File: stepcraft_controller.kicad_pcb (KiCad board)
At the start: 2 copper layers, 68 x 55 mm, 70 parts, among them J1 USB, J10 4th Axle, J11 Input2 Select, J2 Probe, J3 Spindle, J4 OutSelect, J6 Relay select, J7 Serial, J8 ISP, J9 X1, SW1 RST, U1 CP2102N-A01-GQFN24, U2 ADuM1201BR, U3 ADuM1201BR, U4 ATMEGA328P-AU, Y1 Crystal

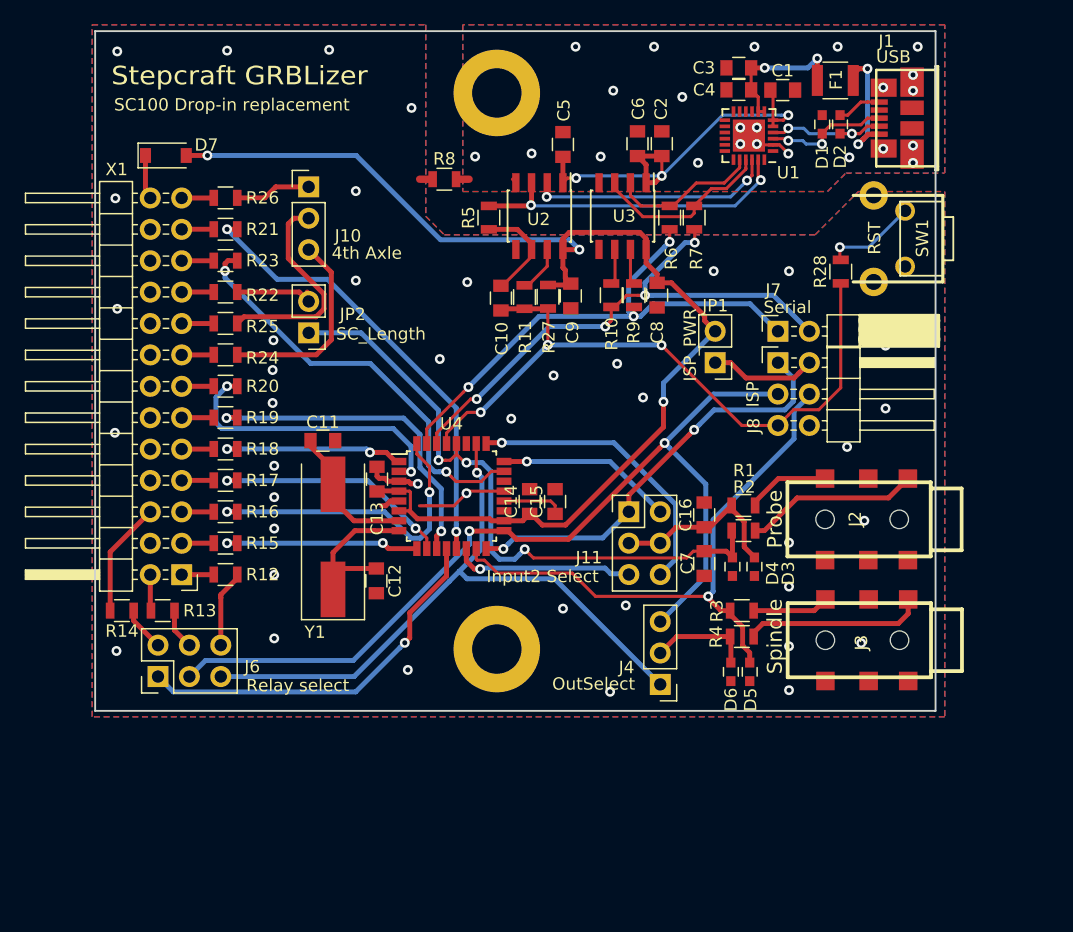
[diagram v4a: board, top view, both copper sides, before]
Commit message: Fix Diode symbol (was reversed), input dcouple caps value, X1 caps value, minor routing improvement.
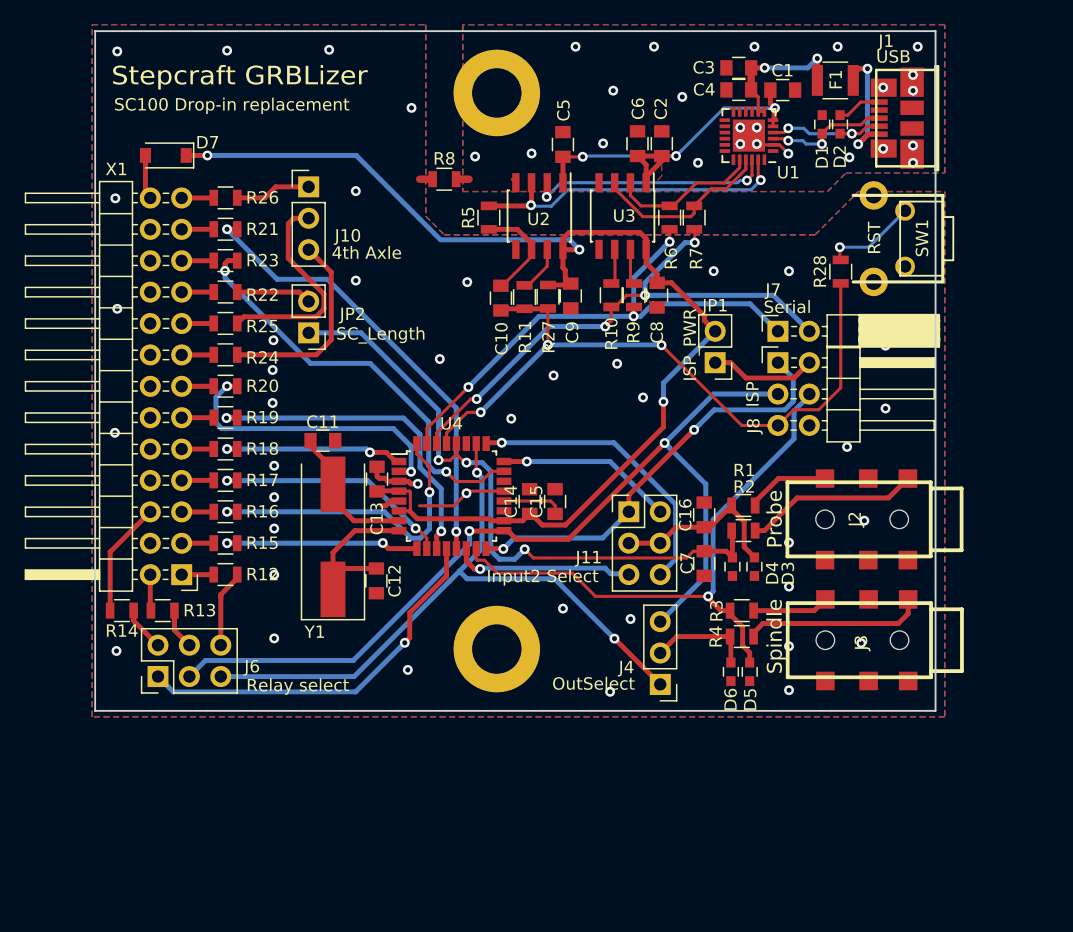
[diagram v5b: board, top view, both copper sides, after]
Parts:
- C11, C12: value 100n -> 22p
- C16, C7: value 100n -> 10n
- D7: value SCHOTTKY -> D_Schottky
- turned D7 to 180 degrees
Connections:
- D7 pad 1: /SC_VCC_5V -> +5V
- D7 pad 2: +5V -> /SC_VCC_5V
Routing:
- net +5VP: track 35.5 -> 32.9 mm
- net /A3: vias 1 -> 2

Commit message: Fix TRS jack pinning Improve some of the scuffy routing...
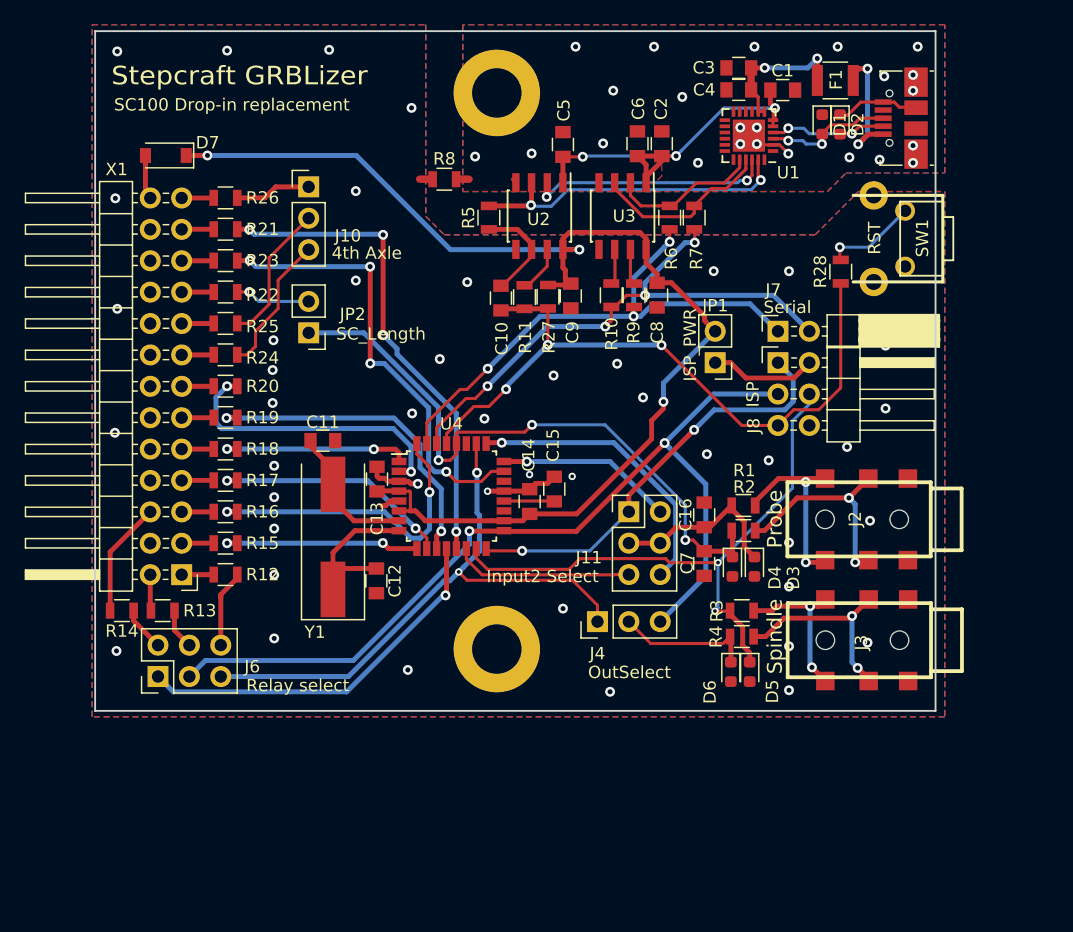
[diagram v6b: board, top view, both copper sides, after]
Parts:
- D1, D2, D3, D4, D5, D6: value D_TVS -> TVS Diode; footprint Capacitors_SMD:C_0603 -> Diode_SMD:D_0603_1608Metric
- J1: footprint iotta_footprints:conn_usb_B_micro_smd -> iotta_footprints:USB_Micro-B_2_Holes
- moved J4 7.18 mm to (180.6, 132.8), turned to 90 degrees
- moved C15 1.01 mm to (177.2, 122.1)
- moved J1 0.88 mm to (205.2, 92.1)
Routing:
- net Net-(J2-Pad2): track 6.73 -> 15.2 mm, vias 0 -> 2
- net Net-(J3-Pad2): track 6.18 -> 12.7 mm, vias 0 -> 2
- net /A3: track 54.2 -> 47.6 mm
- net Net-(J10-Pad2): track 17.4 -> 11.5 mm
- net Net-(J10-Pad3): track 16.2 -> 11.4 mm
- net Net-(J2-Pad1): track 14.1 -> 17.5 mm, vias 0 -> 2
- net /D9: track 36.7 -> 39.8 mm, vias 2 -> 4
- net /SpinDir/Cool: track 8.64 -> 11.6 mm
- net GND: track 7.93 -> 10.8 mm
- net /A0: track 34.1 -> 36.7 mm, vias 2 -> 4
- net /A5: track 53.4 -> 51.5 mm
- net Net-(J3-Pad1): track 14.6 -> 16.4 mm, vias 0 -> 2
- net GNDD: track 14.7 -> 13.3 mm, vias 41 -> 45
- net Net-(C15-Pad1): track 5.03 -> 4.08 mm
- net +5V: track 99.2 -> 98.4 mm
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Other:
- board text added: "Rev 1.1 2017-2022"
- board text removed: "Rev 1.0 2017"

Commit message: Some more minor routing improvements
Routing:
- net +5V: track 98.4 -> 103.4 mm, vias 3 -> 5
- net /D13_SCK: track 75.1 -> 80.0 mm, vias 2 -> 3
- net /A2: track 23.6 -> 21.4 mm
- net /A1: track 14.3 -> 15.5 mm
- net GNDD: vias 45 -> 54
- net /AVR_TX: vias 3 -> 4

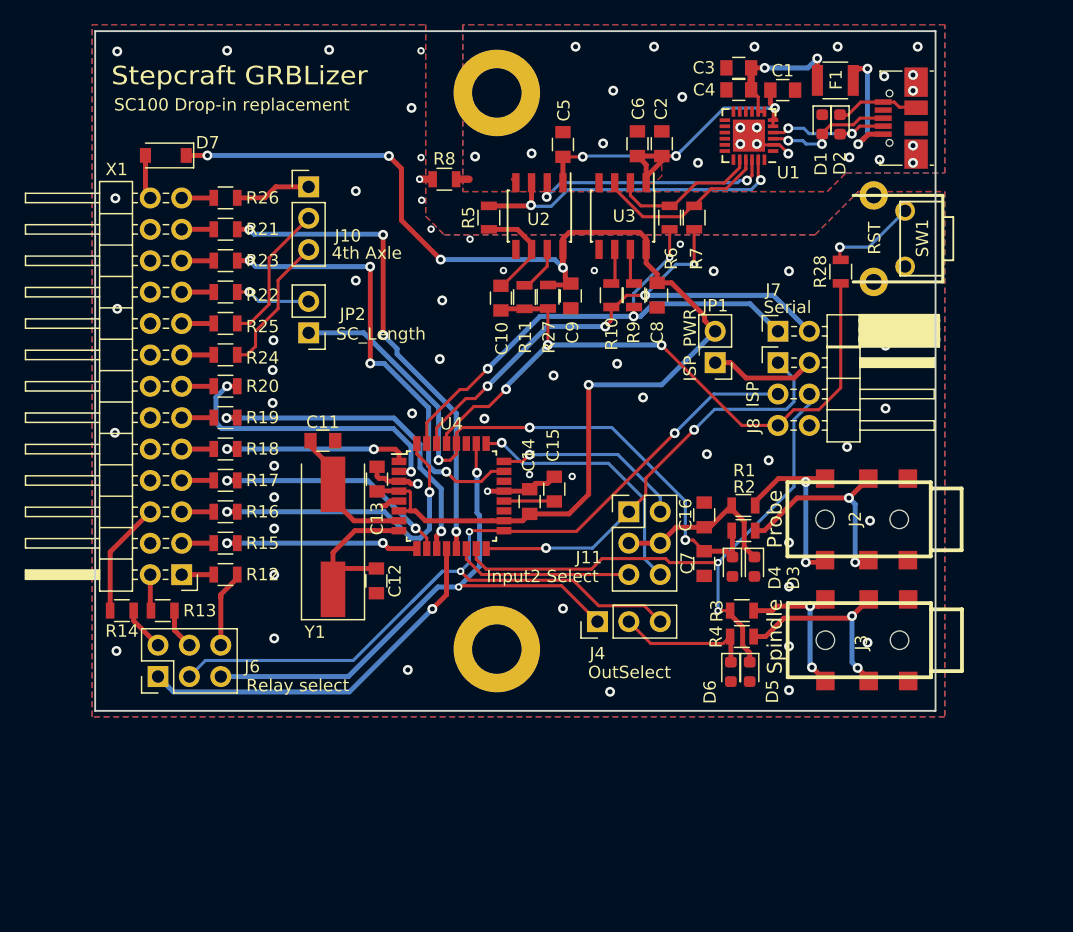
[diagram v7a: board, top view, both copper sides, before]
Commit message: Update project to KiCad v8
- remove all references to external footprints/symbols (close issue #3)
- update footprints to new standard footprint
- add components mgf partnos and LCSC part# for all non standard parts
- shrink PCB outline by 2x0.25mm (for a better fit in machine)
- improve routing
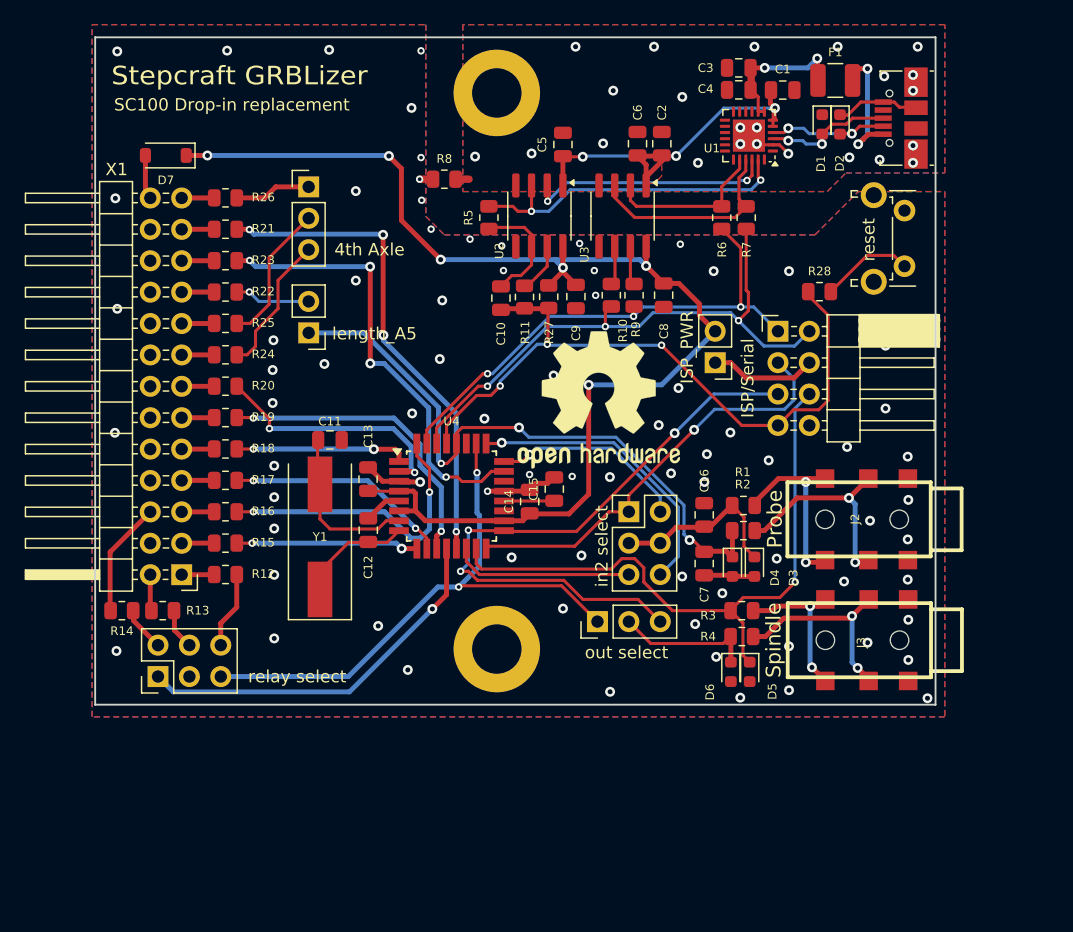
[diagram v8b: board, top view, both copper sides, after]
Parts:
- removed J7: Serial, Pin_Headers:Pin_Header_Angled_2x01_Pitch2.54mm
- added REF**: OSHW-Logo2_14.6x12mm_SilkScreen, Symbol:OSHW-Logo2_14.6x12mm_SilkScreen, F.Cu at (180.8, 114.8)
- added REF**: OSHW-Logo2_14.6x12mm_SilkScreen, Symbol:OSHW-Logo2_14.6x12mm_SilkScreen, B.Cu at (169.6, 112.5)
- C1, C10, C11, C12, C13, C14, C15, C16, C2, C3, C4, C5, C6, C7, C8, C9: footprint Capacitors_SMD:C_0805 -> Capacitor_SMD:C_0805_2012Metric
- D1, D2, D3, D4, D5, D6: value TVS Diode -> Littelfuse PESD0603-240
- D7: value D_Schottky -> 1N5819W; footprint Diodes_SMD:D_SOD-123 -> Diode_SMD:D_SOD-123
- F1: footprint Resistors_SMD:R_1210 -> Fuse:Fuse_1210_3225Metric
- J1: value USB -> UPDATE TO USB C
- J10: footprint Pin_Headers:Pin_Header_Straight_1x03_Pitch2.54mm -> Connector_PinHeader_2.54mm:PinHeader_1x03_P2.54mm_Vertical
- J11: value Input2 Select -> in2 select; footprint Pin_Headers:Pin_Header_Straight_2x03_Pitch2.54mm -> Connector_PinHeader_2.54mm:PinHeader_2x03_P2.54mm_Vertical
- J4: value OutSelect -> out select; footprint Pin_Headers:Pin_Header_Straight_1x03_Pitch2.54mm -> Connector_PinHeader_2.54mm:PinHeader_1x03_P2.54mm_Vertical
- J6: value Relay select -> relay select; footprint Pin_Headers:Pin_Header_Straight_2x03_Pitch2.54mm -> Connector_PinHeader_2.54mm:PinHeader_2x03_P2.54mm_Vertical
- J8: value ISP -> ISP/Serial; footprint Pin_Headers:Pin_Header_Angled_2x03_Pitch2.54mm -> Connector_PinHeader_2.54mm:PinHeader_2x04_P2.54mm_Horizontal
- JP1: footprint Pin_Headers:Pin_Header_Straight_1x02_Pitch2.54mm -> Connector_PinHeader_2.54mm:PinHeader_1x02_P2.54mm_Vertical
- JP2: value SC_Length -> length_A5; footprint Pin_Headers:Pin_Header_Straight_1x02_Pitch2.54mm -> Connector_PinHeader_2.54mm:PinHeader_1x02_P2.54mm_Vertical
- R1, R10, R11, R12, R13, R14, R15, R16, R17, R18, R19, R2, R20, R21, R22, R23, R24, R25, R26, R27, R28, R3, R4, R5, R6, R7, R8, R9: footprint Resistors_SMD:R_0805 -> Resistor_SMD:R_0805_2012Metric
- SW1: value RST -> reset; footprint iotta_footprints:TACTILE_SWITCH_VERTICAL_6MM -> Button_Switch_THT:SW_Tactile_SPST_Angled_PTS645Vx58-2LFS
- U1: value CP2102N-A01-GQFN24 -> CP2102N; footprint Housings_DFN_QFN:QFN-24-1EP_4x4mm_Pitch0.5mm -> Package_DFN_QFN:QFN-24-1EP_4x4mm_P0.5mm_EP2.6x2.6mm
- U2, U3: footprint Housings_SOIC:SOIC-8_3.9x4.9mm_Pitch1.27mm -> Package_SO:SOIC-8_3.9x4.9mm_P1.27mm
- U4: footprint Housings_QFP:LQFP-32_7x7mm_Pitch0.8mm -> Package_QFP:TQFP-32_7x7mm_P0.8mm
- Y1: value Crystal -> 16MHz; footprint Crystals:Crystal_SMD_HC49-SD -> Crystal:Crystal_SMD_HC49-SD
- moved R6 4.21 mm to (190.7, 100.1)
- moved R7 4.21 mm to (192.7, 100.1)
- moved C12 4.15 mm to (162.1, 125.4), turned to 90 degrees
- moved J8 2.54 mm to (195.2, 109.3)
- moved R28 2.36 mm to (198.6, 106.1), turned to 0 degrees
- moved SW1 2.27 mm to (205.5, 99.5), turned to -90 degrees
- moved Y1 1.06 mm to (158.2, 125.9)
- moved C13 0.73 mm to (162.1, 121.3)
- moved C11 0.58 mm to (159.0, 118.1)
- moved C8 0.53 mm to (186.0, 106.4)
- moved C9 0.42 mm to (178.9, 106.5)
- moved R27 0.06 mm to (176.7, 106.5)
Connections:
- net /SpinDir/Cool renamed /SpinDir/Cool
- J1 pad 4: Net-(J1-Pad4) -> unconnected-(J1-ID-Pad4)
- J6 pad 3: /D13_SCK -> unconnected-(J6-P3-Pad3)
- J8 pad 1: /D12_MISO -> /AVR_TX
- J8 pad 2: Net-(J8-Pad2) -> /AVR_RX
- J8 pad 3: /D13_SCK -> /D12_MISO
- J8 pad 4: /D11_MOSI -> Net-(J8-Pin_4)
- J8 pad 5: /AVR_RST -> /D13_SCK
- J8 pad 6: GNDD -> /D11_MOSI
- J9 pad 15: Net-(J9-Pad15) -> unconnected-(J9-P15-Pad15)
- J9 pad 17: Net-(J9-Pad17) -> unconnected-(J9-P17-Pad17)
- JP1 pad 1: Net-(J8-Pad2) -> Net-(J8-Pin_4)
- U1 pad 1: Net-(U1-Pad1) -> unconnected-(U1-RI/CLK-Pad1)
- U1 pad 10: Net-(U1-Pad10) -> unconnected-(U1-NC-Pad10)
- U1 pad 11: Net-(U1-Pad11) -> unconnected-(U1-GPIO.3-Pad11)
- U1 pad 12: Net-(U1-Pad12) -> unconnected-(U1-GPIO.2-Pad12)
- U1 pad 13: Net-(U1-Pad13) -> unconnected-(U1-GPIO.1-Pad13)
- U1 pad 14: Net-(U1-Pad14) -> unconnected-(U1-GPIO.0-Pad14)
- U1 pad 15: Net-(U1-Pad15) -> unconnected-(U1-~{SUSPENDb}-Pad15)
- U1 pad 16: Net-(U1-Pad16) -> unconnected-(U1-NC-Pad16)
- U1 pad 17: Net-(U1-Pad17) -> unconnected-(U1-SUSPEND-Pad17)
- U1 pad 18: Net-(U1-Pad18) -> unconnected-(U1-CTS-Pad18)
- U1 pad 19: Net-(U1-Pad19) -> unconnected-(U1-RTS-Pad19)
- U1 pad 24: Net-(U1-Pad24) -> unconnected-(U1-DCD-Pad24)
- U1 pad 9: Net-(U1-Pad9) -> unconnected-(U1-~{RSTb}-Pad9)
- U4 pad 19: Net-(U4-Pad19) -> unconnected-(U4-ADC6-Pad19)
- U4 pad 22: Net-(U4-Pad22) -> unconnected-(U4-ADC7-Pad22)
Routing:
- net /D13_SCK: track 80.0 -> 51.0 mm
- net Net-(J8-Pin_4): track 0.00 -> 8.65 mm
- net Net-(J8-Pad2): track 8.65 -> 0.00 mm
- net /AVR_XTAL2: track 14.4 -> 7.75 mm
- net GNDD: track 13.3 -> 18.6 mm, vias 54 -> 79
- net /D4: track 23.8 -> 19.7 mm
- net /D11_MOSI: track 47.7 -> 51.5 mm, vias 2 -> 1
- net Net-(U1-TXD): track 14.4 -> 16.9 mm
- net /A2: track 21.4 -> 23.8 mm
- net /AVR_TX: track 44.0 -> 42.2 mm, vias 4 -> 3
- net +5VP: track 32.9 -> 31.1 mm
- net /D7: track 26.7 -> 25.0 mm
- net /D5: track 16.4 -> 14.8 mm
- net /D6: track 19.8 -> 18.2 mm
- net /D3: track 15.6 -> 14.0 mm
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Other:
- board size 68 x 55 mm -> 68 x 54 mm
- net class Default removed
- board text added: "Rev 1.3 CC-BY (c) 2017-24"
- board text added: "https://github.com/eflukx/Stepcraft-GRBLizer"
- board text removed: "Rev 1.1 2017-2022"
